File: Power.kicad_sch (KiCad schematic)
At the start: 3 parts

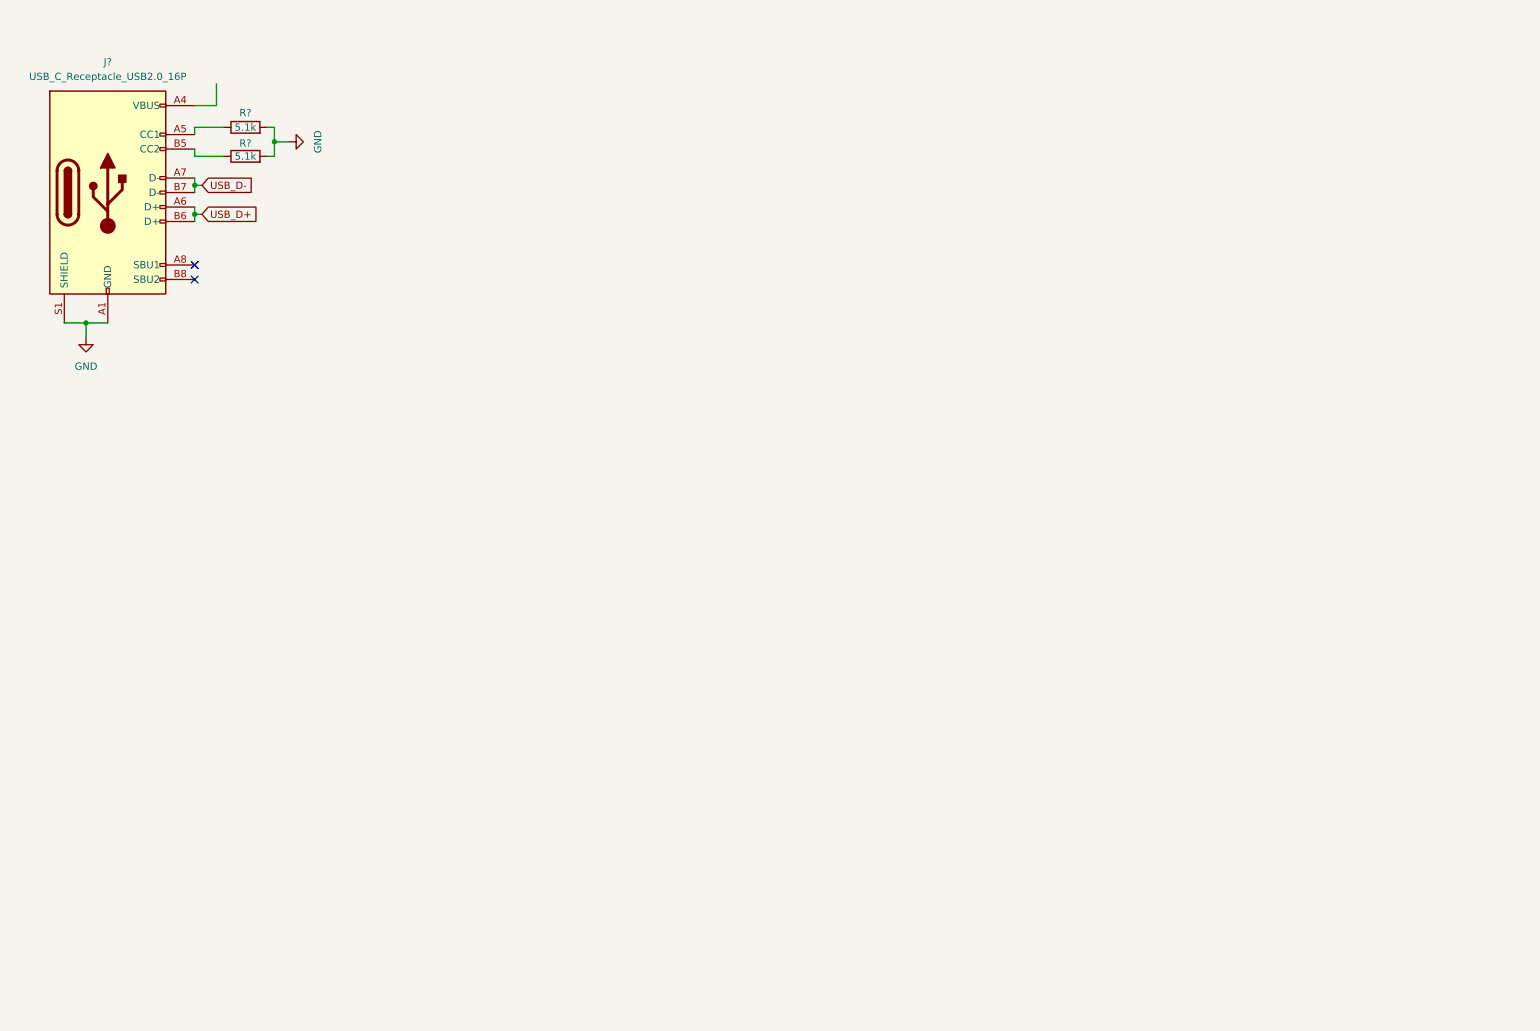
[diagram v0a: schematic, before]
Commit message: Added Power Components
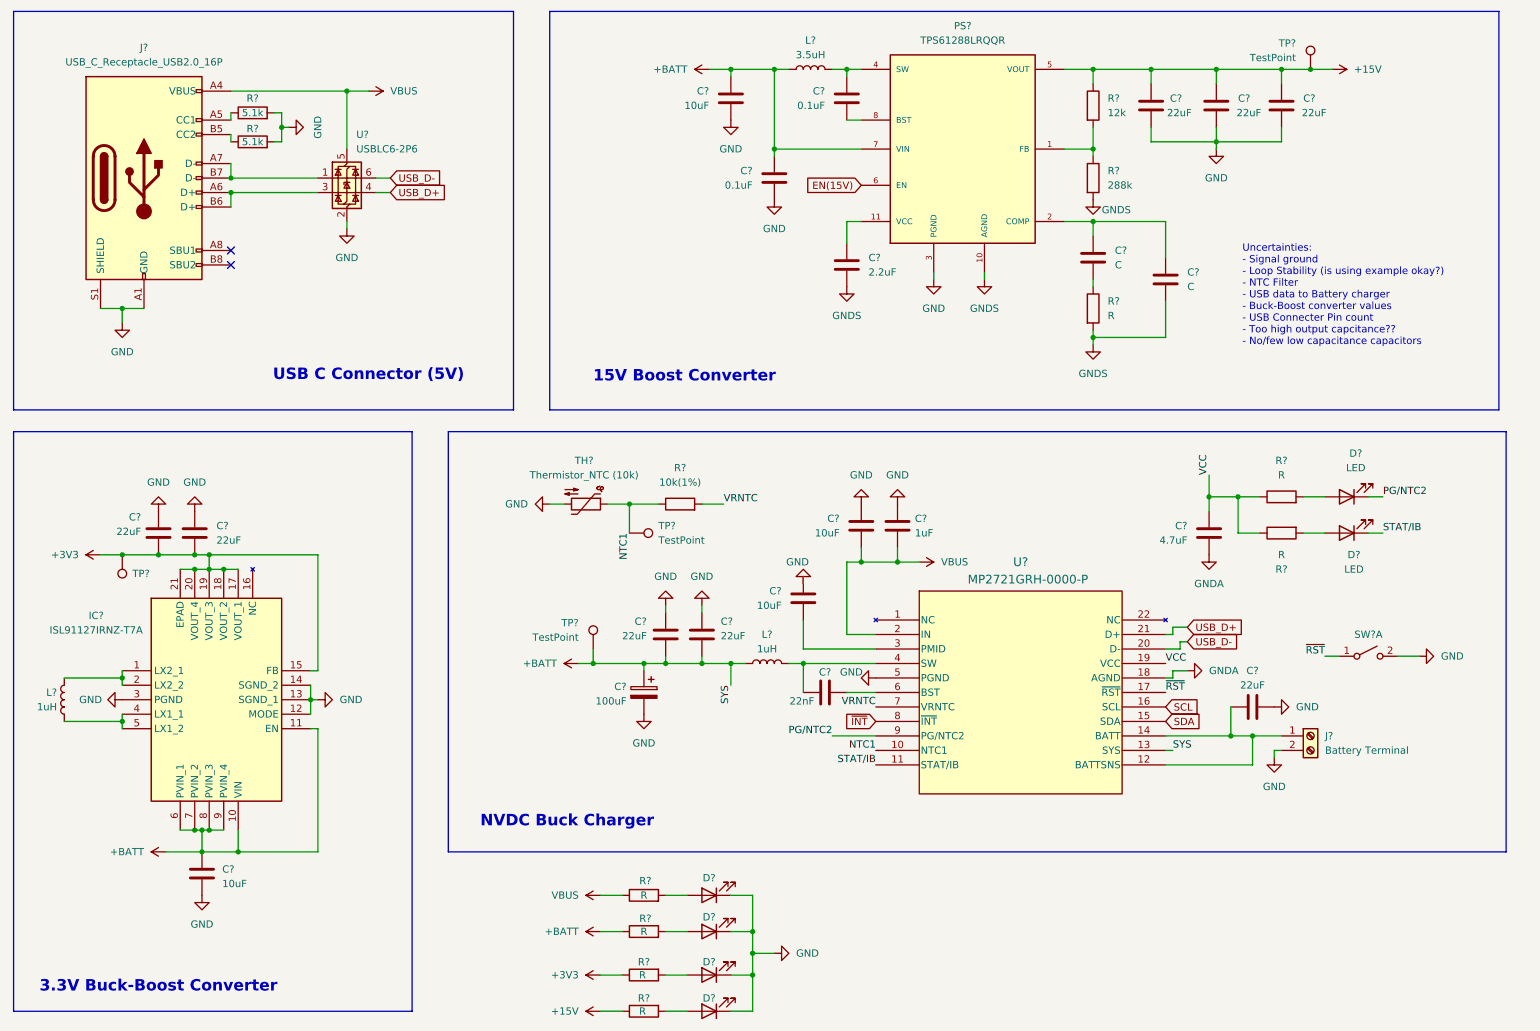
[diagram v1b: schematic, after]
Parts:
- added C? (x2): 0.1uF, symbol Device:C
- added C? (x4): 10uF, symbol Device:C
- added C? (x8): 22uF, symbol Device:C
- added C? (x2): C, symbol Device:C
- added C?: 4.7uF, symbol Device:C
- added C?: 1uF, symbol Device:C
- added C?: 22nF, symbol Device:C
- added C?: 100uF, symbol Device:C_Polarized
- added C?: 2.2uF, symbol Device:C
- added D? (x6): LED, symbol Device:LED
- added IC?: ISL91127IRNZ-T7A, QFN50P400X400X100-21N, symbol ISL91127IRNZ-T7A:ISL91127IRNZ-T7A
- added J?: Battery Terminal, symbol Connector:Screw_Terminal_01x02
- added L? (x2): 1uH, symbol Device:L
- added L?: 3.5uH, symbol Device:L
- added PS?: TPS61288LRQQR, TPS61288LRQQR:CONV_TPS61288LRQQR, symbol TPS61288LRQQR:TPS61288LRQQR
- added R? (x7): R, symbol Device:R
- added R?: 10k(1%), symbol Device:R
- added R?: 12k, symbol Device:R
- added R?: 288k, symbol Device:R
- added SW?: SW_DPST_x2, symbol Switch:SW_DPST_x2
- added TH?: Thermistor_NTC (10k), symbol Device:Thermistor_NTC
- added TP? (x4): TestPoint, symbol Connector:TestPoint
- added U?: MP2721GRH-0000-P, QFN-22_MP2721_MNP, symbol MP2721GRH-0000-P:MP2721GRH-0000-P
- added U?: USBLC6-2P6, Package_TO_SOT_SMD:SOT-666, symbol Power_Protection:USBLC6-2P6
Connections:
- net GND: now also C?.1, C?.1, C?.1, C?.1, C?.1, C?.2, C?.2, C?.2, C?.2, C?.2, C?.2, C?.2, C?.2, C?.2, C?.2, D?.1 (K), D?.1 (K), D?.1 (K), D?.1 (K), IC?.12 (MODE), IC?.13 (SGND_1), IC?.14 (SGND_2), IC?.3 (PGND), J?.2 (Pin_2), PS?.3 (PGND), SW?.2 (B), TH?.2, U?.2 (GND), U?.5 (PGND)
- net USB_D+: now also U?.21 (D+), U?.4 (I/O2); no longer J?.A6 (D+), J?.B6 (D+)
- net USB_D-: now also U?.20 (D-), U?.6 (I/O1); no longer J?.A7 (D-), J?.B7 (D-)
- net VBUS: now reaches J?.A4 (VBUS), J?.A9 (VBUS), J?.B4 (VBUS), J?.B9 (VBUS)
- net VBUS: now also C?.1, C?.2, R?.1, U?.2 (IN), U?.5 (VBUS)
- new net: D?.2 (A), R?.2 (x6)
- new net: PS?.1 (FB), R?.1, R?.2
- new net: C?.1, PS?.11 (VCC)
- new net: C?.1, C?.1, PS?.2 (COMP)
- new net: C?.1, L?.2, PS?.4 (SW), PS?.9 (SW)
- new net: C?.2, PS?.8 (BST)
- new net: C?.1, L?.2, U?.4 (SW)
- new net: C?.2, J?.1 (Pin_1), U?.12 (BATTSNS), U?.14 (BATT)
- new net: C?.1, U?.3 (PMID)
- new net: C?.2, U?.6 (BST)
- new net: C?.2, R?.1
- new net: IC?.1 (LX2_1), IC?.2 (LX2_2), L?.1
- new net: IC?.4 (LX1_1), IC?.5 (LX1_2), L?.2
- new net: J?.A6 (D+), J?.B6 (D+), U?.3 (I/O2)
- new net: J?.A7 (D-), J?.B7 (D-), U?.1 (I/O1)
- new net +15V: C?.1, C?.1, C?.1, PS?.5 (VOUT), R?.1, R?.1, TP?.1
- new net +3V3: C?.2, C?.2, IC?.15 (FB), IC?.17 (VOUT_1), IC?.18 (VOUT_2), IC?.19 (VOUT_3), IC?.20 (VOUT_4), IC?.21 (EPAD), R?.1, TP?.1
- new net +BATT: C?.1, C?.1, C?.1, C?.1, C?.1, C?.2, IC?.10 (VIN), IC?.11 (EN), IC?.6 (PVIN_1), IC?.7 (PVIN_2), IC?.8 (PVIN_3), IC?.9 (PVIN_4), L?.1, L?.1, PS?.7 (VIN), R?.1, TP?.1, U?.13 (SYS)
- new net EN(15V): PS?.6 (EN)
- new net GNDA: C?.2, U?.18 (AGND)
- new net GNDS: C?.2, C?.2, PS?.10 (AGND), R?.2, R?.2
- new net NTC1: R?.1, TH?.1, TP?.1, U?.10 (NTC1)
- new net PG/NTC2: D?.1 (K), U?.9 (PG/NTC2)
- new net SCL: U?.16 (SCL)
- new net SDA: U?.15 (SDA)
- new net STAT/IB: D?.1 (K), U?.11 (STAT/IB)
- new net VCC: C?.1, R?.1, R?.1, U?.19 (VCC)
- new net VRNTC: R?.2, U?.7 (VRNTC)
- new net ~{INT}: U?.8 (~{INT})
- new net ~{RST}: SW?.1 (A), U?.17 (~{RST})
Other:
- note added: "15V Boost Converter"
- note added: "3.3V Buck-Boost Converter"
- note added: "NVDC Buck Charger"
- note added: "USB C Connector (5V)"
- note added: "Uncertainties: - Signal ground - Loop Stability (is using example okay?) - NTC Filter - USB data to Battery charger - Buck-Boost converter values - USB Connecter Pin count - Too high output capcitance?? - No/few low capacitance capacitors"
- moved on the sheet: J?, R?
